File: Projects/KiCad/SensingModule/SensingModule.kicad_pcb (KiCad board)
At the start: 2 copper layers, 110 x 95 mm, 22 parts, among them J1 Conn_01x04_Pin, J2 Conn_01x04_Socket, J3 Micro_SD_Card_Det_Hirose_DM3AT, U1 NUCLEO-F303K8, U2 MCP2562-E-P, U3 24LC256

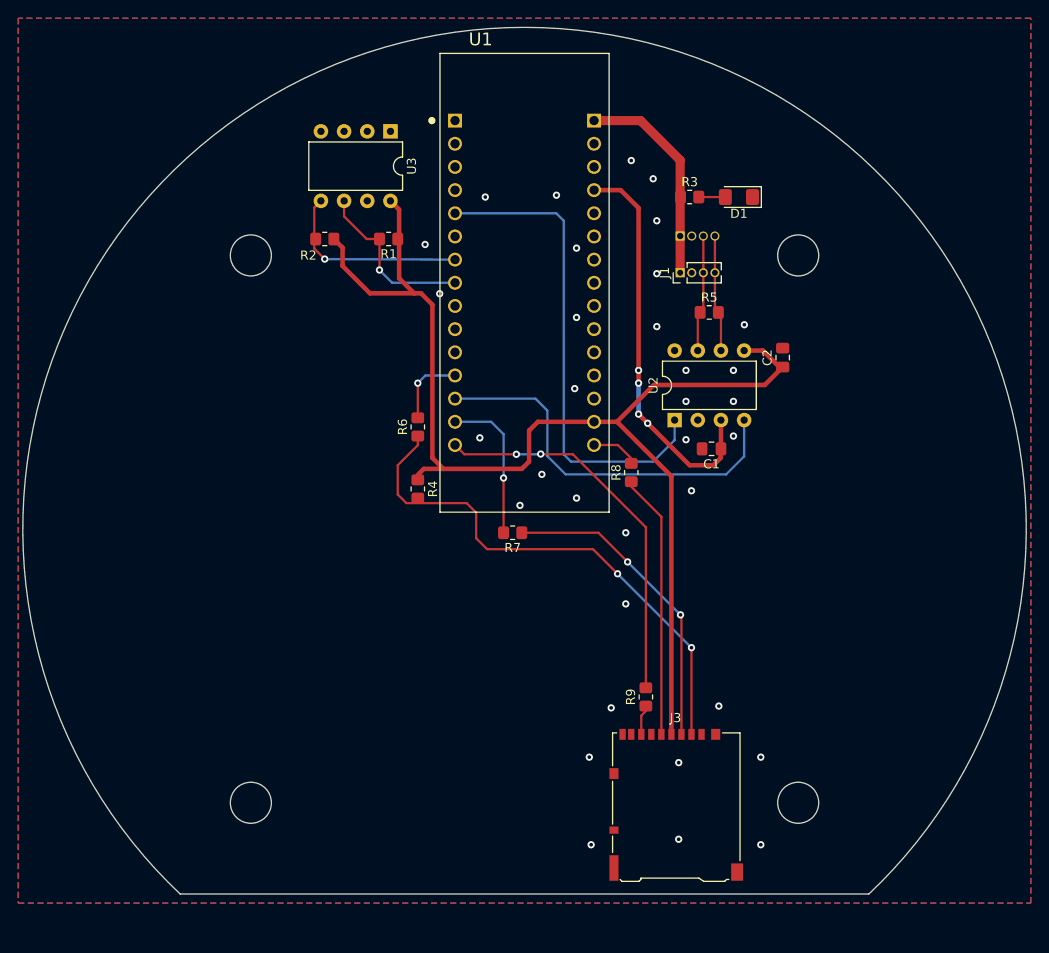
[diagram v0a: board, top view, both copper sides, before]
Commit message: 通信モジュールを一旦作成
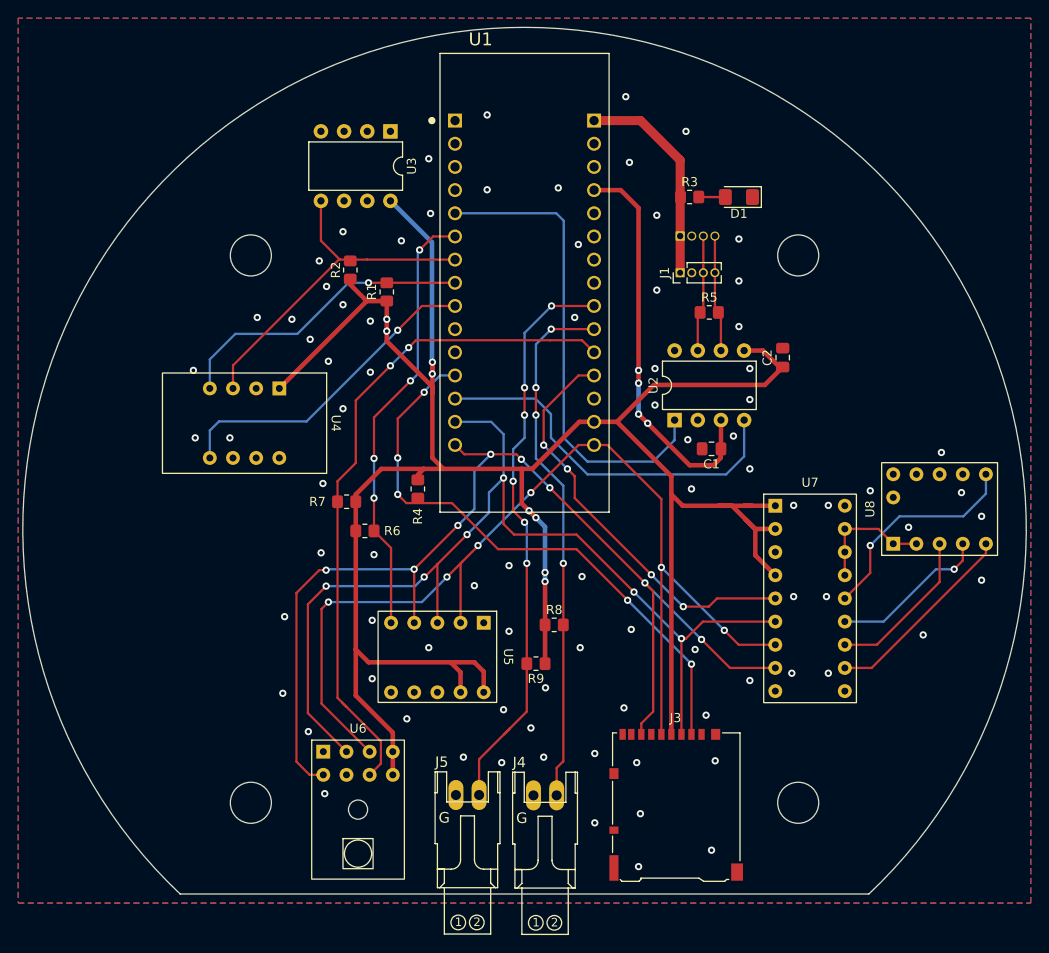
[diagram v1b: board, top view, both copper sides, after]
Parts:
- added J4: Conn_01x02_Pin, Hirose_Connector:Hirose_DF1B, F.Cu at (150.8, 138.0)
- added J5: Conn_01x02_Pin, Hirose_Connector:Hirose_DF1B, F.Cu at (142.2, 138.0)
- added U4: ~, Akizuki_BNO055_Module:BNO055, F.Cu at (126.7, 93.4)
- added U5: ~, StrawberryLinux_ADXL375_Module:ADXL375, F.Cu at (145.4, 119.0)
- added U6: ~, StrawberryLinux_LPS33HW_Module:LPS33HW, F.Cu at (130.2, 135.8)
- added U7: ~, StrawberryLinux_TUX0304_Module:TUX0304, F.Cu at (179.8, 112.6)
- added U8: ~, StrawberryLinux_ICM20948_Module:ICM20948, F.Cu at (194.0, 102.8)
- R6, R7: value 22Ω -> 4.7kΩ
- R8, R9: value 22Ω -> 10kΩ
- moved R8 18.7 mm to (151.8, 115.5), turned to 0 degrees
- moved R7 18.5 mm to (129.0, 102.0)
- moved R6 12.8 mm to (131.0, 105.2), turned to 0 degrees
- moved R9 12.6 mm to (149.8, 119.8), turned to 180 degrees
- moved R1 5.80 mm to (133.4, 79.0), turned to 90 degrees
- moved R2 4.40 mm to (129.4, 76.6), turned to 90 degrees
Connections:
- J3 pad 7: Net-(J3-DAT0) -> SPI_MISO
- R6 pad 1: SPI_CS_SD -> +3.3V
- R6 pad 2: Net-(U1A-PA8) -> SPI_CS_ADXL
- R7 pad 1: SPI_MOSI -> +3.3V
- R7 pad 2: Net-(U1A-PB5) -> SPI_CS_LPS
- R8 pad 1: SPI_SCLK -> +3.3V
- R8 pad 2: Net-(U1B-PB3) -> THERMISTOR1
- R9 pad 1: Net-(J3-DAT0) -> +3.3V
- R9 pad 2: SPI_MISO -> THERMISTOR2
- U1 pad 3_12: Net-(U1A-PA8) -> SPI_CS_SD
- U1 pad 3_14: Net-(U1A-PB5) -> SPI_MOSI
- U1 pad 3_6: unconnected-(U1A-PB0-Pad3_6) -> SPI_CS_ADXL
- U1 pad 3_9: unconnected-(U1A-PB1-Pad3_9) -> BNO_RESET
- U1 pad 4_10: unconnected-(U1B-PA3-Pad4_10) -> THERMISTOR1
- U1 pad 4_11: unconnected-(U1B-PA1-Pad4_11) -> SPI_CS_LPS
- U1 pad 4_12: unconnected-(U1B-PA0-Pad4_12) -> SPI_CS_ICM
- U1 pad 4_15: Net-(U1B-PB3) -> SPI_SCLK
- U1 pad 4_9: unconnected-(U1B-PA4-Pad4_9) -> THERMISTOR2
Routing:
- net +3.3V: track 133.3 -> 264.4 mm, vias 0 -> 8
- net SPI_SCLK: track 28.5 -> 114.5 mm, vias 0 -> 6
- net SPI_MOSI: track 34.3 -> 114.7 mm, vias 2 -> 6
- net SPI_MISO: track 41.7 -> 120.8 mm, vias 2 -> 8
- net SPI_CS_LPS: track 0.00 -> 74.5 mm, vias 0 -> 2
- net THERMISTOR2: track 0.00 -> 63.7 mm, vias 0 -> 6
- net THERMISTOR1: track 0.00 -> 58.0 mm, vias 0 -> 4
- net SPI_CS_ADXL: track 0.00 -> 48.3 mm, vias 0 -> 4
- net SPI_CS_ICM: track 0.00 -> 45.4 mm, vias 0 -> 4
- net BNO_RESET: track 0.00 -> 35.5 mm, vias 0 -> 1
- net Net-(U7-CSB): track 0.00 -> 24.1 mm, vias 0 -> 1
- net Net-(U7-MISOB): track 0.00 -> 21.7 mm
- net Net-(U7-MOSIB): track 0.00 -> 17.5 mm, vias 0 -> 1
- net I2C_SDA: track 21.5 -> 39.0 mm, vias 1 -> 0
- net Net-(U7-SCKB): track 0.00 -> 17.4 mm
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
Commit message: ビアを修正
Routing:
- net +3.3V: vias 8 -> 6

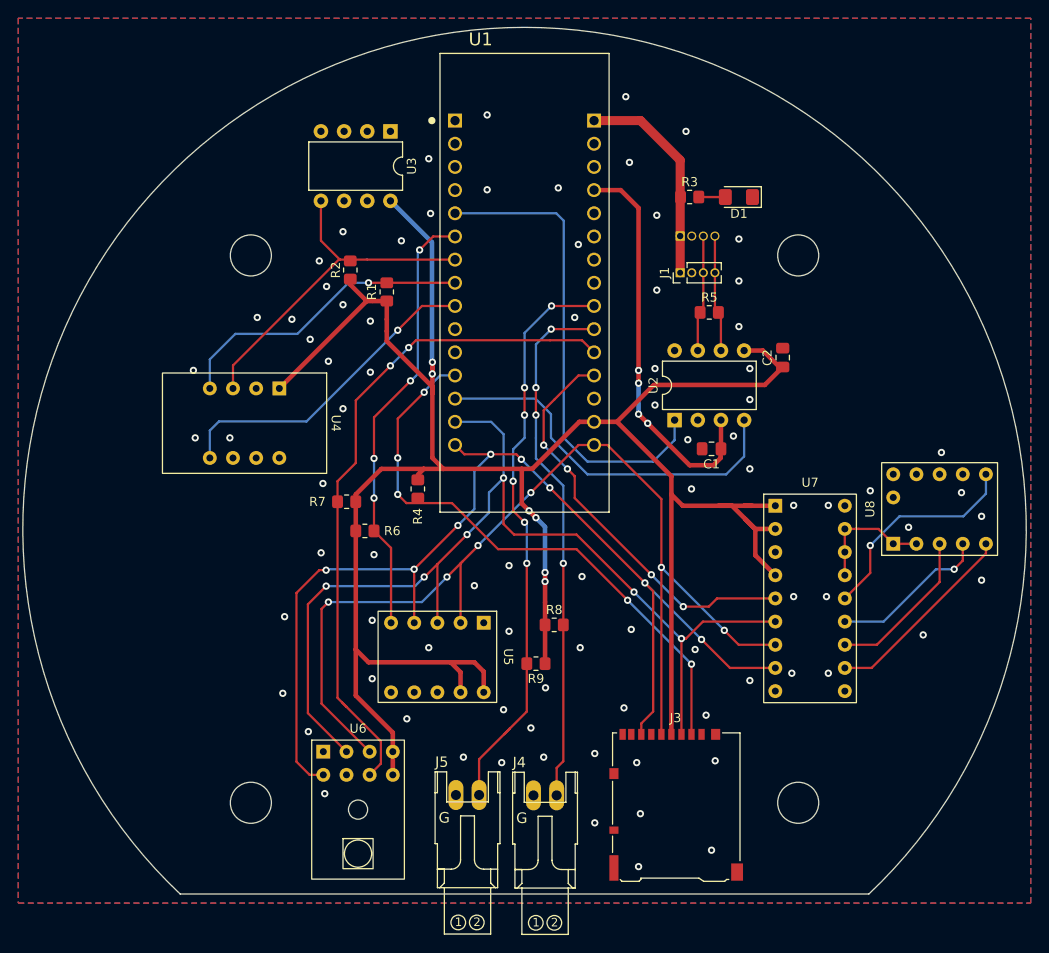
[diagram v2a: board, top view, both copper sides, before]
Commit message: フライトモジュールのKiCadを追加
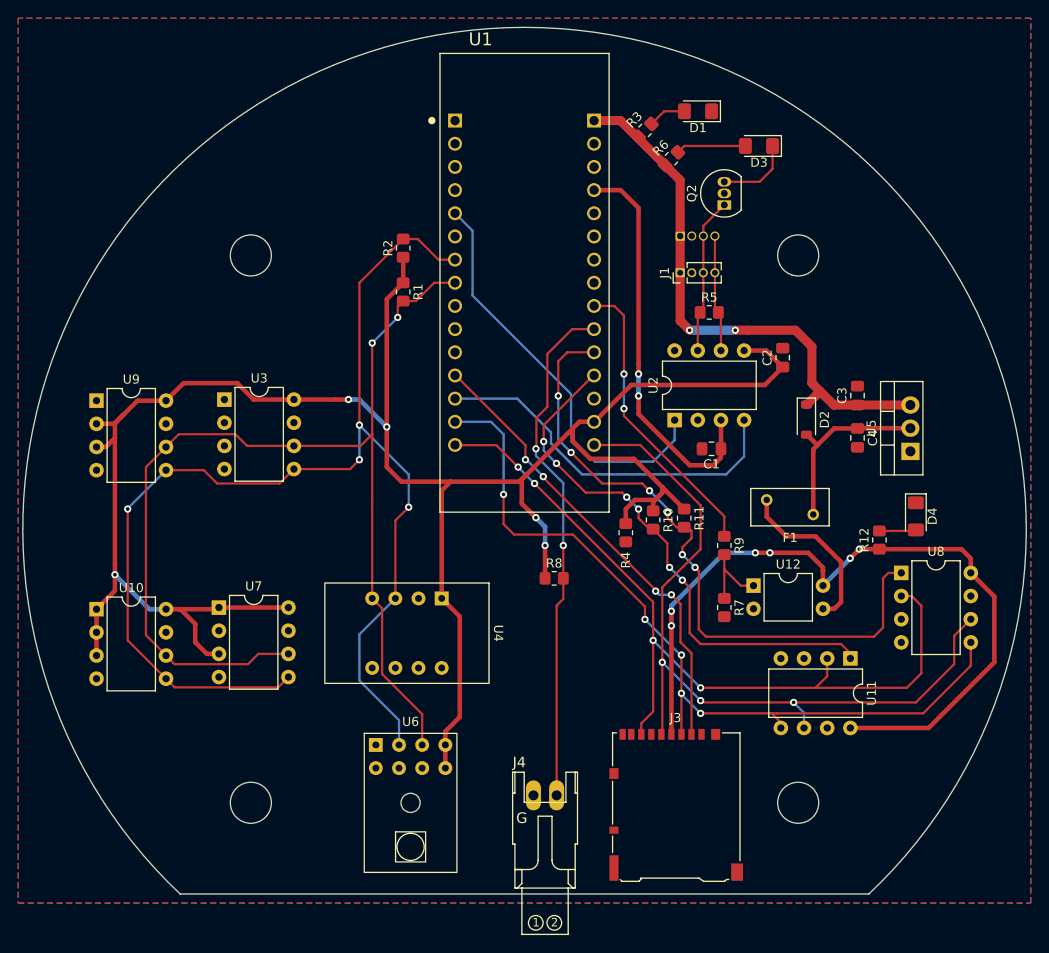
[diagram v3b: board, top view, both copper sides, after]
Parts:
- removed J5: Conn_01x02_Pin, Hirose_Connector:Hirose_DF1B
- added C3: 0.1μF, Capacitor_SMD:C_0805_2012Metric_Pad1.18x1.45mm_HandSolder, F.Cu at (185.0, 90.4)
- added C4: 0.1μF, Capacitor_SMD:C_0805_2012Metric_Pad1.18x1.45mm_HandSolder, F.Cu at (185.0, 95.0)
- added D2: 1N4007, Diode_SMD:D_SOD-123, F.Cu at (179.4, 93.0)
- added D3: LED, LED_SMD:LED_1206_3216Metric_Pad1.42x1.75mm_HandSolder, F.Cu at (174.2, 63.0)
- added D4: LED, LED_SMD:LED_1206_3216Metric_Pad1.42x1.75mm_HandSolder, F.Cu at (191.4, 103.6)
- added F1: Polyfuse, Fuse:Fuse_BelFuse_0ZRE0005FF_L8.3mm_W3.8mm, F.Cu at (180.2, 103.4)
- added Q2: DTC143E, Package_TO_SOT_THT:TO-92_Inline, F.Cu at (170.4, 69.5)
- added R10: 4.7kΩ, Resistor_SMD:R_0805_2012Metric_Pad1.20x1.40mm_HandSolder, F.Cu at (162.6, 104.0)
- added R11: 4.7kΩ, Resistor_SMD:R_0805_2012Metric_Pad1.20x1.40mm_HandSolder, F.Cu at (166.0, 103.8)
- added R12: 1kΩ, Resistor_SMD:R_0805_2012Metric_Pad1.20x1.40mm_HandSolder, F.Cu at (187.4, 106.2)
- added U10: 24LC1025, Package_DIP:DIP-8_W7.62mm, F.Cu at (101.6, 113.8)
- added U11: MB85RS2MT, Package_DIP:DIP-8_W7.62mm, F.Cu at (184.2, 119.2)
- added U12: TLP222A, Package_DIP:DIP-4_W7.62mm, F.Cu at (173.6, 111.2)
- added U9: 24LC1025, Package_DIP:DIP-8_W7.62mm, F.Cu at (101.6, 90.9)
- R6: value 4.7kΩ -> 2kΩ
- R7: value 4.7kΩ -> 120Ω
- R9: value 10kΩ -> 120Ω
- U3: value 24LC256 -> 24LC1025
- U5: value ~ -> LT1584-3.3; footprint StrawberryLinux_ADXL375_Module:ADXL375 -> Package_TO_SOT_THT:TO-220-3_Vertical
- U7: value ~ -> 24LC1025; footprint StrawberryLinux_TUX0304_Module:TUX0304 -> Package_DIP:DIP-8_W7.62mm
- U8: value ~ -> MB85RS2MT; footprint StrawberryLinux_ICM20948_Module:ICM20948 -> Package_DIP:DIP-8_W7.62mm
- moved U7 64.8 mm to (115.0, 113.6)
- moved R6 52.9 mm to (164.6, 64.4), turned to 45 degrees
- moved U5 50.6 mm to (190.8, 96.5), turned to 90 degrees
- moved R7 43.0 mm to (170.4, 113.6), turned to -90 degrees
- moved U3 34.6 mm to (115.6, 90.8), turned to 0 degrees
- moved U4 29.1 mm to (144.5, 116.4)
- moved R9 24.4 mm to (170.4, 106.8), turned to -90 degrees
- moved R4 23.3 mm to (159.6, 105.4)
- moved D1 10.4 mm to (167.5, 59.2)
- moved R3 8.79 mm to (161.7, 61.3), turned to 45 degrees
- moved U8 8.16 mm to (189.8, 109.8), turned to 0 degrees
- moved R2 6.28 mm to (135.2, 74.2)
- moved U6 5.81 mm to (136.0, 135.0)
- moved R8 5.10 mm to (151.8, 110.4)
- moved R1 1.80 mm to (135.2, 79.0), turned to -90 degrees
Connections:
- net THERMISTOR1 renamed THERMISTOR
- J3 pad 4: +3.3V -> MEMORY_POWER
- R6 pad 1: +3.3V -> +12V
- R6 pad 2: SPI_CS_ADXL -> Net-(D3-A)
- R7 pad 1: +3.3V -> Net-(R7-Pad1)
- R7 pad 2: SPI_CS_LPS -> GND
- R9 pad 1: +3.3V -> MEMORY_POWER_CONTROL
- R9 pad 2: THERMISTOR2 -> Net-(R7-Pad1)
- U1 pad 3_6: SPI_CS_ADXL -> unconnected-(U1A-PB0-Pad3_6)
- U1 pad 3_9: BNO_RESET -> unconnected-(U1A-PB1-Pad3_9)
- U1 pad 4_11: SPI_CS_LPS -> SPI_CS_FRAM0
- U1 pad 4_12: SPI_CS_ICM -> SPI_CS_FRAM1
- U1 pad 4_9: THERMISTOR2 -> MEMORY_POWER_CONTROL
- U3 pad 3: GND -> +3.3V
- U4 pad 5: BNO_RESET -> unconnected-(U4-RESET-Pad5)
- U5 pad 2: SPI_SCLK -> Net-(D2-A)
- U5 pad 3: SPI_MOSI -> +12V
- U6 pad 2: SPI_MOSI -> I2C_SDA
- U6 pad 3: SPI_SCLK -> I2C_SCL
- U6 pad 5: SPI_MISO -> GND
- U6 pad 7: SPI_CS_LPS -> unconnected-(U6-~CS-Pad7)
- U7 pad 2: +3.3V -> GND
- U7 pad 3: GND -> +3.3V
- U7 pad 4: +3.3V -> GND
- U7 pad 5: SPI_CS_ICM -> I2C_SDA
- U7 pad 6: SPI_MOSI -> I2C_SCL
- U7 pad 7: SPI_SCLK -> GND
- U7 pad 8: SPI_MISO -> +3.3V
- U8 pad 1: +1V8 -> SPI_CS_FRAM0
- U8 pad 2: +1V8 -> SPI_MISO
- U8 pad 3: Net-(U7-SCKB) -> GND
- U8 pad 4: Net-(U7-MOSIB) -> GND
- U8 pad 5: Net-(U7-MISOB) -> SPI_MOSI
- U8 pad 6: Net-(U7-CSB) -> SPI_SCLK
- U8 pad 7: unconnected-(U8-AUX_CL-Pad7) -> GND
- U8 pad 8: unconnected-(U8-AUX_DA-Pad8) -> MEMORY_POWER
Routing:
- net I2C_SDA: track 39.0 -> 137.6 mm, vias 0 -> 4
- net I2C_SCL: track 33.5 -> 122.0 mm, vias 1 -> 2
- net MEMORY_POWER: track 0.00 -> 85.3 mm, vias 0 -> 6
- net SPI_CS_LPS: track 74.5 -> 0.00 mm, vias 2 -> 0
- net SPI_CS_FRAM0: track 0.00 -> 72.8 mm, vias 0 -> 6
- net THERMISTOR2: track 63.7 -> 0.00 mm, vias 6 -> 0
- net SPI_CS_FRAM1: track 0.00 -> 58.9 mm, vias 0 -> 6
- net SPI_CS_ADXL: track 48.3 -> 0.00 mm, vias 4 -> 0
- net SPI_CS_ICM: track 45.4 -> 0.00 mm, vias 4 -> 0
- net +12V: track 23.6 -> 61.1 mm, vias 0 -> 2
- net BNO_RESET: track 35.5 -> 0.00 mm, vias 1 -> 0
- net MEMORY_POWER_CONTROL: track 0.00 -> 32.5 mm, vias 0 -> 2
- net SPI_MISO: track 120.8 -> 89.9 mm, vias 8 -> 4
- net SPI_SCLK: track 114.5 -> 85.8 mm, vias 6 -> 3
- net SPI_MOSI: track 114.7 -> 90.1 mm, vias 6 -> 5
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
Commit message: バスパワーの接続を修正
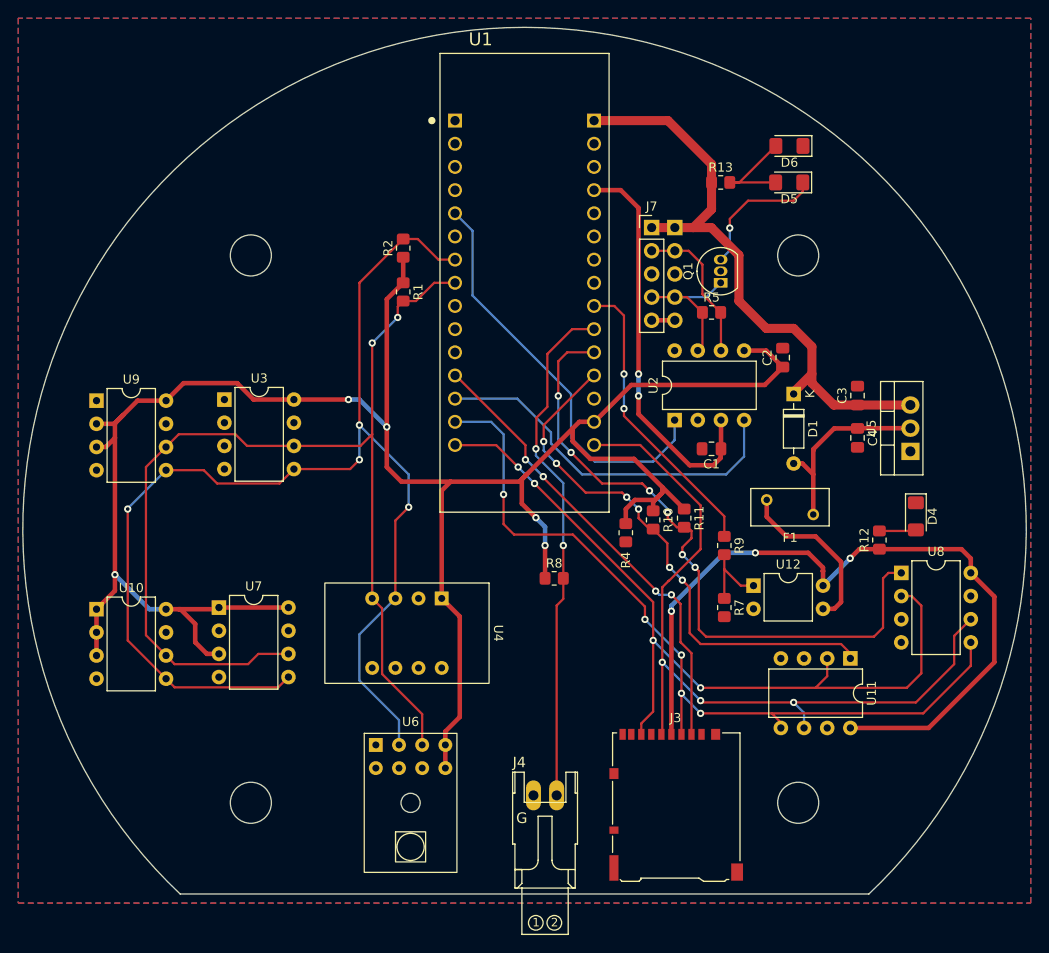
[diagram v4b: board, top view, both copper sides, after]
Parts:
- removed D2: 1N4007, Diode_SMD:D_SOD-123
- removed D3: LED, LED_SMD:LED_1206_3216Metric_Pad1.42x1.75mm_HandSolder
- removed J1: Conn_01x04_Pin, Connector_PinHeader_1.27mm:PinHeader_1x04_P1.27mm_Vertical
- removed J2: Conn_01x04_Socket, Connector_PinSocket_1.27mm:PinSocket_1x04_P1.27mm_Vertical
- removed Q2: DTC143E, Package_TO_SOT_THT:TO-92_Inline
- removed R3, R6: 2kΩ, Resistor_SMD:R_0805_2012Metric_Pad1.20x1.40mm_HandSolder
- added D5: LED, LED_SMD:LED_1206_3216Metric_Pad1.42x1.75mm_HandSolder, F.Cu at (177.5, 67.0)
- added D6: LED, LED_SMD:LED_1206_3216Metric_Pad1.42x1.75mm_HandSolder, F.Cu at (177.5, 63.0)
- added J5: Conn_01x05_Socket, Connector_PinSocket_2.54mm:PinSocket_1x05_P2.54mm_Vertical, B.Cu at (165.0, 72.0)
- added J7: Conn_01x05_Pin, Connector_PinHeader_2.54mm:PinHeader_1x05_P2.54mm_Vertical, F.Cu at (162.4, 72.0)
- added Q1: DTC143E, Package_TO_SOT_THT:TO-92_Inline, F.Cu at (170.0, 78.0)
- added R13: 2kΩ, Resistor_SMD:R_0805_2012Metric_Pad1.20x1.40mm_HandSolder, F.Cu at (170.0, 67.0)
- D1: value LED -> 1N4148; footprint LED_SMD:LED_1206_3216Metric_Pad1.42x1.75mm_HandSolder -> Diode_THT:D_DO-35_SOD27_P7.62mm_Horizontal
- moved D1 32.7 mm to (178.0, 90.2), turned to -90 degrees
- moved R5 0.25 mm to (169.0, 81.2)
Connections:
- C4 pad 1: Net-(D2-A) -> Net-(D1-A)
- D1 pad 1: GND -> +12V
- F1 pad 1: Net-(D2-A) -> Net-(D1-A)
- U4 pad 2: GND -> (no net)
- U5 pad 2: Net-(D2-A) -> Net-(D1-A)
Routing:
- net Net-(D2-A): track 20.4 -> 0.00 mm
- net Net-(D1-A): track 4.18 -> 21.4 mm
- net Net-(D5-K): track 0.00 -> 15.1 mm, vias 0 -> 1
- net Net-(D5-A): track 0.00 -> 11.7 mm
- net Net-(D3-K): track 8.39 -> 0.00 mm
- net Net-(D3-A): track 7.69 -> 0.00 mm
- net +12V: track 61.1 -> 67.2 mm, vias 2 -> 0
- net CAN_L: track 12.8 -> 16.4 mm
- net +5V: track 44.1 -> 46.6 mm
- net CAN_H: track 17.2 -> 15.7 mm
- net SPI_CS_FRAM1: track 58.9 -> 57.8 mm
- net SPI_MOSI: track 90.1 -> 89.5 mm
- net MEMORY_POWER: vias 6 -> 3

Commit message: RCを解決
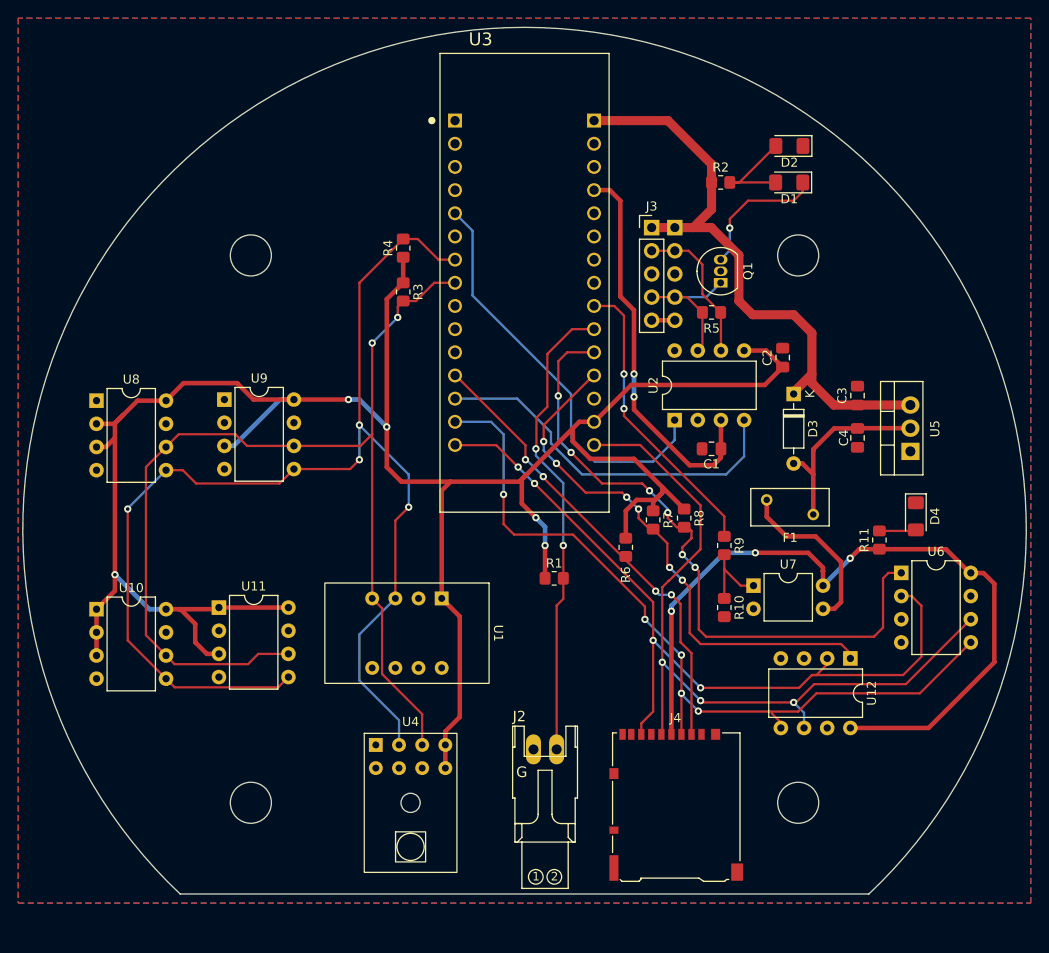
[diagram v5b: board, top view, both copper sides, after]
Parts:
- moved J2 5.04 mm to (150.8, 133.0)
- moved R6 1.60 mm to (159.6, 107.0)
- renumbered D5 to D1, D6 to D2, D1 to D3, J5 to J1, J4 to J2, J7 to J3, J3 to J4, R8 to R1, R7 to R10, R12 to R11, R13 to R2, R1 to R3, R2 to R4, R4 to R6, R10 to R7, R11 to R8, U4 to U1, U7 to U11, U11 to U12, U1 to U3, U6 to U4, U8 to U6, U12 to U7, U9 to U8, U3 to U9
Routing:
- net +3.3V: track 243.7 -> 254.9 mm
- net THERMISTOR: track 56.7 -> 51.7 mm
- net SPI_MISO: track 89.9 -> 87.9 mm
- net SPI_SCLK: track 85.7 -> 83.9 mm
- net SPI_MOSI: track 89.5 -> 87.9 mm
- net +12V: track 67.2 -> 68.1 mm
- net +5V: track 46.6 -> 45.9 mm
